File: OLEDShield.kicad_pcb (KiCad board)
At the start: 2 copper layers, 14 parts, among them P1 CONN_5X2, P2 CONN_5X2

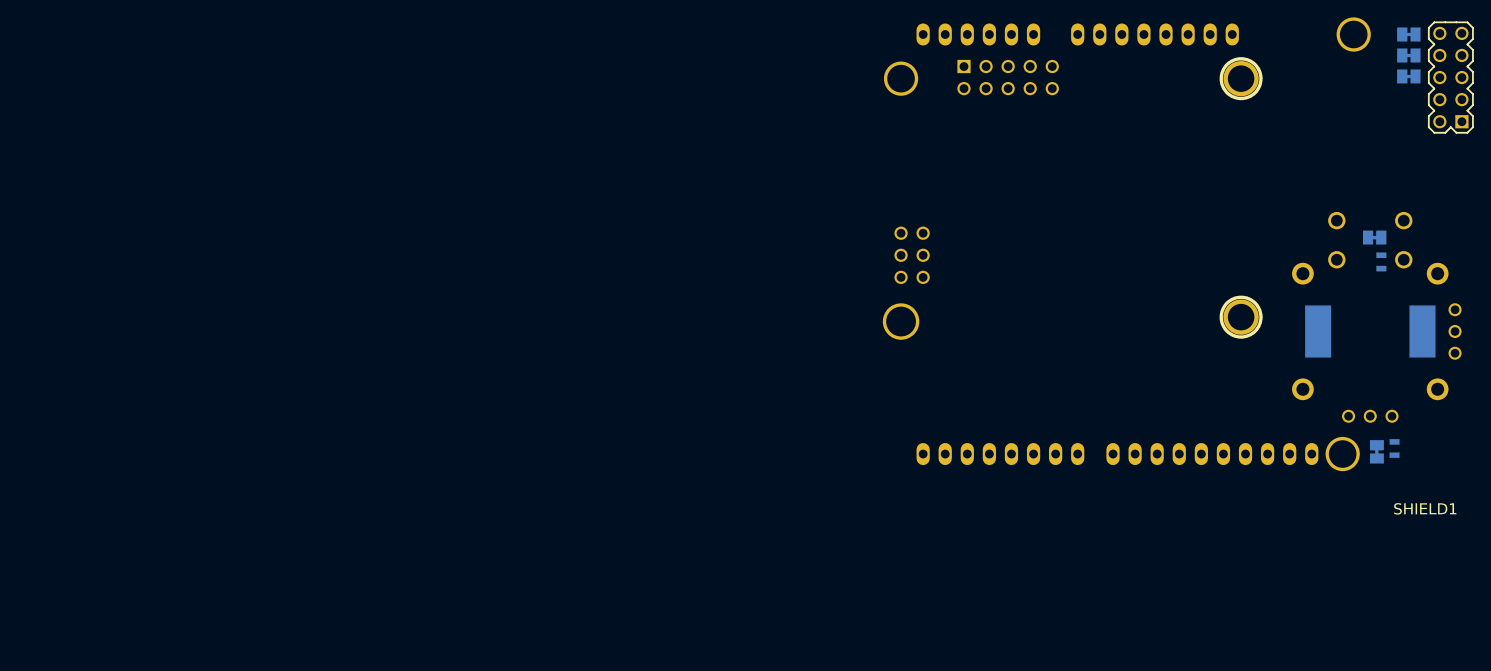
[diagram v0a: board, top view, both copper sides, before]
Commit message: Board largely done, no silkscreen labels yet
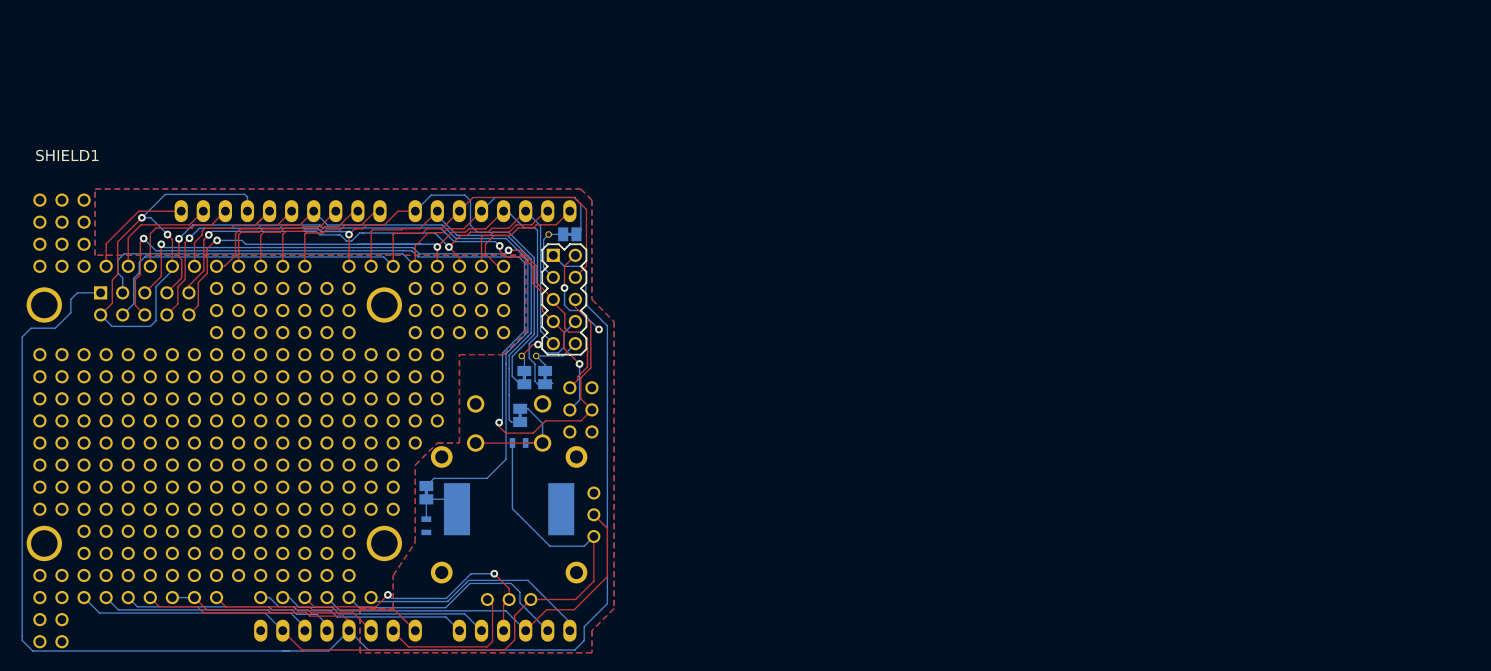
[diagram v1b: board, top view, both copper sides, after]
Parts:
- removed the 1PIN at (359.2, 238.3)
- added 1PIN: P***, 1pin_prototyping, F.Cu at (221.0, 227.3)
- added 1PIN: P***, 1pin_prototyping, F.Cu at (259.1, 252.7)
- added 1PIN: P***, 1pin_prototyping, F.Cu at (243.8, 255.3)
- added 1PIN: P***, 1pin_prototyping, F.Cu at (243.8, 247.7)
- added 1PIN: P***, 1pin_prototyping, F.Cu at (238.8, 247.7)
- added 1PIN: P***, 1pin_prototyping, F.Cu at (241.3, 247.7)
- added 1PIN: P***, 1pin_prototyping, F.Cu at (246.4, 247.7)
- added 1PIN: P***, 1pin_prototyping, F.Cu at (248.9, 247.7)
- added 1PIN: P***, 1pin_prototyping, F.Cu at (251.5, 247.7)
- added 1PIN: P***, 1pin_prototyping, F.Cu at (254.0, 247.7)
- added 1PIN: P***, 1pin_prototyping, F.Cu at (254.0, 250.2)
- added 1PIN: P***, 1pin_prototyping, F.Cu at (251.5, 250.2)
- added 1PIN: P***, 1pin_prototyping, F.Cu at (259.1, 250.2)
- added 1PIN: P***, 1pin_prototyping, F.Cu at (248.9, 250.2)
- added 1PIN: P***, 1pin_prototyping, F.Cu at (246.4, 250.2)
- added 1PIN: P***, 1pin_prototyping, F.Cu at (243.8, 250.2)
- added 1PIN: P***, 1pin_prototyping, F.Cu at (241.3, 250.2)
- added 1PIN: P***, 1pin_prototyping, F.Cu at (238.8, 250.2)
- added 1PIN: P***, 1pin_prototyping, F.Cu at (238.8, 252.7)
- added 1PIN: P***, 1pin_prototyping, F.Cu at (241.3, 252.7)
- added 1PIN: P***, 1pin_prototyping, F.Cu at (243.8, 252.7)
- added 1PIN: P***, 1pin_prototyping, F.Cu at (246.4, 252.7)
- added 1PIN: P***, 1pin_prototyping, F.Cu at (248.9, 252.7)
- added 1PIN: P***, 1pin_prototyping, F.Cu at (259.1, 247.7)
- added 1PIN: P***, 1pin_prototyping, F.Cu at (251.5, 252.7)
- added 1PIN: P***, 1pin_prototyping, F.Cu at (254.0, 252.7)
- added 1PIN: P***, 1pin_prototyping, F.Cu at (236.2, 247.7)
- added 1PIN: P***, 1pin_prototyping, F.Cu at (233.7, 247.7)
- added 1PIN: P***, 1pin_prototyping, F.Cu at (231.1, 247.7)
- added 1PIN: P***, 1pin_prototyping, F.Cu at (228.6, 247.7)
- added 1PIN: P***, 1pin_prototyping, F.Cu at (226.1, 247.7)
- added 1PIN: P***, 1pin_prototyping, F.Cu at (223.5, 247.7)
- added 1PIN: P***, 1pin_prototyping, F.Cu at (221.0, 247.7)
- added 1PIN: P***, 1pin_prototyping, F.Cu at (221.0, 245.1)
- added 1PIN: P***, 1pin_prototyping, F.Cu at (259.1, 255.3)
- added 1PIN: P***, 1pin_prototyping, F.Cu at (223.5, 245.1)
- added 1PIN: P***, 1pin_prototyping, F.Cu at (226.1, 245.1)
- added 1PIN: P***, 1pin_prototyping, F.Cu at (228.6, 245.1)
- added 1PIN: P***, 1pin_prototyping, F.Cu at (231.1, 245.1)
- added 1PIN: P***, 1pin_prototyping, F.Cu at (233.7, 245.1)
- added 1PIN: P***, 1pin_prototyping, F.Cu at (236.2, 245.1)
- added 1PIN: P***, 1pin_prototyping, F.Cu at (236.2, 242.6)
- added 1PIN: P***, 1pin_prototyping, F.Cu at (233.7, 242.6)
- added 1PIN: P***, 1pin_prototyping, F.Cu at (231.1, 242.6)
- added 1PIN: P***, 1pin_prototyping, F.Cu at (228.6, 242.6)
- added 1PIN: P***, 1pin_prototyping, F.Cu at (259.1, 257.8)
- added 1PIN: P***, 1pin_prototyping, F.Cu at (223.5, 242.6)
- added 1PIN: P***, 1pin_prototyping, F.Cu at (221.0, 242.6)
- added 1PIN: P***, 1pin_prototyping, F.Cu at (226.1, 242.6)
- added 1PIN: P***, 1pin_prototyping, F.Cu at (259.1, 270.5)
- added 1PIN: P***, 1pin_prototyping, F.Cu at (256.5, 270.5)
- added 1PIN: P***, 1pin_prototyping, F.Cu at (254.0, 270.5)
- added 1PIN: P***, 1pin_prototyping, F.Cu at (251.5, 270.5)
- added 1PIN: P***, 1pin_prototyping, F.Cu at (248.9, 270.5)
- added 1PIN: P***, 1pin_prototyping, F.Cu at (246.4, 270.5)
- added 1PIN: P***, 1pin_prototyping, F.Cu at (241.3, 270.5)
- added 1PIN: P***, 1pin_prototyping, F.Cu at (259.1, 260.4)
- added 1PIN: P***, 1pin_prototyping, F.Cu at (238.8, 270.5)
- added 1PIN: P***, 1pin_prototyping, F.Cu at (236.2, 270.5)
- added 1PIN: P***, 1pin_prototyping, F.Cu at (233.7, 270.5)
- added 1PIN: P***, 1pin_prototyping, F.Cu at (231.1, 270.5)
- added 1PIN: P***, 1pin_prototyping, F.Cu at (228.6, 270.5)
- added 1PIN: P***, 1pin_prototyping, F.Cu at (226.1, 270.5)
- added 1PIN: P***, 1pin_prototyping, F.Cu at (274.3, 232.4)
- added 1PIN: P***, 1pin_prototyping, F.Cu at (271.8, 232.4)
- added 1PIN: P***, 1pin_prototyping, F.Cu at (269.2, 232.4)
- added 1PIN: P***, 1pin_prototyping, F.Cu at (266.7, 232.4)
- added 1PIN: P***, 1pin_prototyping, F.Cu at (261.6, 260.4)
- added 1PIN: P***, 1pin_prototyping, F.Cu at (264.2, 232.4)
- added 1PIN: P***, 1pin_prototyping, F.Cu at (261.6, 232.4)
- added 1PIN: P***, 1pin_prototyping, F.Cu at (259.1, 232.4)
- added 1PIN: P***, 1pin_prototyping, F.Cu at (256.5, 232.4)
- added 1PIN: P***, 1pin_prototyping, F.Cu at (251.5, 232.4)
- added 1PIN: P***, 1pin_prototyping, F.Cu at (248.9, 232.4)
- added 1PIN: P***, 1pin_prototyping, F.Cu at (246.4, 232.4)
- added 1PIN: P***, 1pin_prototyping, F.Cu at (243.8, 232.4)
- added 1PIN: P***, 1pin_prototyping, F.Cu at (241.3, 232.4)
- added 1PIN: P***, 1pin_prototyping, F.Cu at (238.8, 232.4)
- added 1PIN: P***, 1pin_prototyping, F.Cu at (261.6, 257.8)
- added 1PIN: P***, 1pin_prototyping, F.Cu at (231.1, 232.4)
- added 1PIN: P***, 1pin_prototyping, F.Cu at (228.6, 232.4)
- added 1PIN: P***, 1pin_prototyping, F.Cu at (233.7, 232.4)
- added 1PIN: P***, 1pin_prototyping, F.Cu at (236.2, 232.4)
- added 1PIN: P***, 1pin, B.Cu at (221.5, 264.3)
- added 1PIN: P***, 1pin, B.Cu at (260.6, 264.3)
- added 1PIN: P***, 1pin, B.Cu at (260.6, 236.9)
- added 1PIN: P***, 1pin_prototyping, F.Cu at (241.3, 234.9)
- added 1PIN: P***, 1pin_prototyping, F.Cu at (243.8, 234.9)
- added 1PIN: P***, 1pin_prototyping, F.Cu at (261.6, 255.3)
- added 1PIN: P***, 1pin_prototyping, F.Cu at (246.4, 234.9)
- added 1PIN: P***, 1pin_prototyping, F.Cu at (248.9, 234.9)
- added 1PIN: P***, 1pin_prototyping, F.Cu at (251.5, 234.9)
- added 1PIN: P***, 1pin_prototyping, F.Cu at (254.0, 234.9)
- added 1PIN: P***, 1pin_prototyping, F.Cu at (256.5, 234.9)
- added 1PIN: P***, 1pin_prototyping, F.Cu at (241.3, 237.5)
- added 1PIN: P***, 1pin_prototyping, F.Cu at (243.8, 237.5)
- added 1PIN: P***, 1pin_prototyping, F.Cu at (246.4, 237.5)
- added 1PIN: P***, 1pin_prototyping, F.Cu at (248.9, 237.5)
- added 1PIN: P***, 1pin_prototyping, F.Cu at (251.5, 237.5)
- added 1PIN: P***, 1pin_prototyping, F.Cu at (261.6, 247.7)
- added 1PIN: P***, 1pin_prototyping, F.Cu at (254.0, 237.5)
- added 1PIN: P***, 1pin_prototyping, F.Cu at (256.5, 237.5)
- added 1PIN: P***, 1pin_prototyping, F.Cu at (241.3, 240.0)
- added 1PIN: P***, 1pin_prototyping, F.Cu at (243.8, 240.0)
- added 1PIN: P***, 1pin_prototyping, F.Cu at (246.4, 240.0)
- added 1PIN: P***, 1pin_prototyping, F.Cu at (248.9, 240.0)
- added 1PIN: P***, 1pin_prototyping, F.Cu at (251.5, 240.0)
- added 1PIN: P***, 1pin_prototyping, F.Cu at (254.0, 240.0)
- added 1PIN: P***, 1pin_prototyping, F.Cu at (256.5, 240.0)
- added 1PIN: P***, 1pin_prototyping, F.Cu at (226.1, 250.2)
- added 1PIN: P***, 1pin_prototyping, F.Cu at (223.5, 227.3)
- added 1PIN: P***, 1pin_prototyping, F.Cu at (261.6, 250.2)
- added 1PIN: P***, 1pin_prototyping, F.Cu at (221.0, 250.2)
- added 1PIN: P***, 1pin_prototyping, F.Cu at (223.5, 250.2)
- added 1PIN: P***, 1pin_prototyping, F.Cu at (228.6, 250.2)
- added 1PIN: P***, 1pin_prototyping, F.Cu at (231.1, 250.2)
- added 1PIN: P***, 1pin_prototyping, F.Cu at (233.7, 250.2)
- added 1PIN: P***, 1pin_prototyping, F.Cu at (236.2, 250.2)
- added 1PIN: P***, 1pin_prototyping, F.Cu at (238.8, 242.6)
- added 1PIN: P***, 1pin_prototyping, F.Cu at (241.3, 242.6)
- added 1PIN: P***, 1pin_prototyping, F.Cu at (243.8, 242.6)
- added 1PIN: P***, 1pin_prototyping, F.Cu at (246.4, 242.6)
- added 1PIN: P***, 1pin_prototyping, F.Cu at (261.6, 252.7)
- added 1PIN: P***, 1pin_prototyping, F.Cu at (248.9, 242.6)
- added 1PIN: P***, 1pin_prototyping, F.Cu at (251.5, 242.6)
- added 1PIN: P***, 1pin_prototyping, F.Cu at (254.0, 242.6)
- added 1PIN: P***, 1pin_prototyping, F.Cu at (256.5, 242.6)
- added 1PIN: P***, 1pin_prototyping, F.Cu at (264.2, 240.0)
- added 1PIN: P***, 1pin_prototyping, F.Cu at (264.2, 237.5)
- added 1PIN: P***, 1pin_prototyping, F.Cu at (264.2, 234.9)
- added 1PIN: P***, 1pin_prototyping, F.Cu at (266.7, 234.9)
- added 1PIN: P***, 1pin_prototyping, F.Cu at (266.7, 237.5)
- added 1PIN: P***, 1pin_prototyping, F.Cu at (266.7, 240.0)
- added 1PIN: P***, 1pin_prototyping, F.Cu at (256.5, 252.7)
- added 1PIN: P***, 1pin_prototyping, F.Cu at (269.2, 240.0)
- added 1PIN: P***, 1pin_prototyping, F.Cu at (269.2, 237.5)
- added 1PIN: P***, 1pin_prototyping, F.Cu at (269.2, 234.9)
- added 1PIN: P***, 1pin_prototyping, F.Cu at (271.8, 234.9)
- added 1PIN: P***, 1pin_prototyping, F.Cu at (271.8, 237.5)
- added 1PIN: P***, 1pin_prototyping, F.Cu at (271.8, 240.0)
- added 1PIN: P***, 1pin_prototyping, F.Cu at (274.3, 240.0)
- added 1PIN: P***, 1pin_prototyping, F.Cu at (274.3, 237.5)
- added 1PIN: P***, 1pin_prototyping, F.Cu at (274.3, 234.9)
- added 1PIN: P***, 1pin_prototyping, F.Cu at (266.7, 242.6)
- added 1PIN: P***, 1pin_prototyping, F.Cu at (256.5, 250.2)
- added 1PIN: P***, 1pin_prototyping, F.Cu at (266.7, 245.1)
- added 1PIN: P***, 1pin_prototyping, F.Cu at (266.7, 247.7)
- added 1PIN: P***, 1pin_prototyping, F.Cu at (266.7, 250.2)
- added 1PIN: P***, 1pin_prototyping, F.Cu at (264.2, 242.6)
- added 1PIN: P***, 1pin_prototyping, F.Cu at (264.2, 245.1)
- added 1PIN: P***, 1pin_prototyping, F.Cu at (264.2, 247.7)
- added 1PIN: P***, 1pin_prototyping, F.Cu at (264.2, 250.2)
- added 1PIN: P***, 1pin_prototyping, F.Cu at (264.2, 252.7)
- added 1PIN: P***, 1pin_prototyping, F.Cu at (261.6, 242.6)
- added 1PIN: P***, 1pin_prototyping, F.Cu at (259.1, 242.6)
- added 1PIN: P***, 1pin_prototyping, F.Cu at (256.5, 247.7)
- added 1PIN: P***, 1pin_prototyping, F.Cu at (261.6, 245.1)
- added 1PIN: P***, 1pin_prototyping, F.Cu at (259.1, 245.1)
- added 1PIN: P***, 1pin_prototyping, F.Cu at (256.5, 245.1)
- added 1PIN: P***, 1pin_prototyping, F.Cu at (254.0, 245.1)
- added 1PIN: P***, 1pin_prototyping, F.Cu at (251.5, 245.1)
- added 1PIN: P***, 1pin_prototyping, F.Cu at (248.9, 245.1)
- added 1PIN: P***, 1pin_prototyping, F.Cu at (246.4, 245.1)
- added 1PIN: P***, 1pin_prototyping, F.Cu at (243.8, 245.1)
- added 1PIN: P***, 1pin_prototyping, F.Cu at (241.3, 245.1)
- added 1PIN: P***, 1pin_prototyping, F.Cu at (238.8, 245.1)
- added 1PIN: P***, 1pin_prototyping, F.Cu at (256.5, 255.3)
- added 1PIN: P***, 1pin_prototyping, F.Cu at (236.2, 252.7)
- added 1PIN: P***, 1pin_prototyping, F.Cu at (233.7, 252.7)
- added 1PIN: P***, 1pin_prototyping, F.Cu at (231.1, 252.7)
- added 1PIN: P***, 1pin_prototyping, F.Cu at (228.6, 252.7)
- added 1PIN: P***, 1pin_prototyping, F.Cu at (226.1, 252.7)
- added 1PIN: P***, 1pin_prototyping, F.Cu at (223.5, 252.7)
- added 1PIN: P***, 1pin_prototyping, F.Cu at (221.0, 252.7)
- added 1PIN: P***, 1pin_prototyping, F.Cu at (221.0, 255.3)
- added 1PIN: P***, 1pin_prototyping, F.Cu at (223.5, 255.3)
- added 1PIN: P***, 1pin_prototyping, F.Cu at (226.1, 255.3)
- added 1PIN: P***, 1pin_prototyping, F.Cu at (256.5, 257.8)
- added 1PIN: P***, 1pin_prototyping, F.Cu at (228.6, 255.3)
- added 1PIN: P***, 1pin_prototyping, F.Cu at (231.1, 255.3)
- added 1PIN: P***, 1pin_prototyping, F.Cu at (233.7, 255.3)
- added 1PIN: P***, 1pin_prototyping, F.Cu at (236.2, 255.3)
- added 1PIN: P***, 1pin_prototyping, F.Cu at (226.1, 268.0)
- added 1PIN: P***, 1pin_prototyping, F.Cu at (226.1, 232.4)
- added 1PIN: P***, 1pin_prototyping, F.Cu at (223.5, 232.4)
- added 1PIN: P***, 1pin_prototyping, F.Cu at (221.0, 232.4)
- added 1PIN: P***, 1pin_prototyping, F.Cu at (223.5, 268.0)
- added 1PIN: P***, 1pin_prototyping, F.Cu at (221.0, 268.0)
- added 1PIN: P***, 1pin_prototyping, F.Cu at (256.5, 260.4)
- added 1PIN: P***, 1pin_prototyping, F.Cu at (221.0, 270.5)
- added 1PIN: P***, 1pin_prototyping, F.Cu at (223.5, 270.5)
- added 1PIN: P***, 1pin_prototyping, F.Cu at (223.5, 273.1)
- added 1PIN: P***, 1pin_prototyping, F.Cu at (221.0, 273.1)
- added 1PIN: P***, 1pin_prototyping, F.Cu at (223.5, 275.6)
- added 1PIN: P***, 1pin_prototyping, F.Cu at (221.0, 275.6)
- added 1PIN: P***, 1pin_prototyping, F.Cu at (256.5, 265.4)
- added 1PIN: P***, 1pin_prototyping, F.Cu at (256.5, 262.9)
- added 1PIN: P***, 1pin_prototyping, F.Cu at (226.1, 227.3)
- added 1PIN: P***, 1pin_prototyping, F.Cu at (256.5, 268.0)
- added 1PIN: P***, 1pin_prototyping, F.Cu at (236.2, 268.0)
- added 1PIN: P***, 1pin_prototyping, F.Cu at (233.7, 268.0)
- added 1PIN: P***, 1pin_prototyping, F.Cu at (231.1, 268.0)
- added 1PIN: P***, 1pin_prototyping, F.Cu at (228.6, 268.0)
- added 1PIN: P***, 1pin_prototyping, F.Cu at (254.0, 268.0)
- added 1PIN: P***, 1pin_prototyping, F.Cu at (251.5, 268.0)
- added 1PIN: P***, 1pin_prototyping, F.Cu at (248.9, 268.0)
- added 1PIN: P***, 1pin_prototyping, F.Cu at (246.4, 268.0)
- added 1PIN: P***, 1pin_prototyping, F.Cu at (243.8, 268.0)
- added 1PIN: P***, 1pin_prototyping, F.Cu at (226.1, 224.8)
- added 1PIN: P***, 1pin_prototyping, F.Cu at (241.3, 268.0)
- added 1PIN: P***, 1pin_prototyping, F.Cu at (238.8, 268.0)
- added 1PIN: P***, 1pin_prototyping, F.Cu at (254.0, 262.9)
- added 1PIN: P***, 1pin_prototyping, F.Cu at (251.5, 262.9)
- added 1PIN: P***, 1pin_prototyping, F.Cu at (248.9, 262.9)
- added 1PIN: P***, 1pin_prototyping, F.Cu at (246.4, 262.9)
- added 1PIN: P***, 1pin_prototyping, F.Cu at (243.8, 262.9)
- added 1PIN: P***, 1pin_prototyping, F.Cu at (241.3, 262.9)
- added 1PIN: P***, 1pin_prototyping, F.Cu at (238.8, 262.9)
- added 1PIN: P***, 1pin_prototyping, F.Cu at (238.8, 265.4)
- added 1PIN: P***, 1pin_prototyping, F.Cu at (223.5, 224.8)
- added 1PIN: P***, 1pin_prototyping, F.Cu at (241.3, 265.4)
- added 1PIN: P***, 1pin_prototyping, F.Cu at (243.8, 265.4)
- added 1PIN: P***, 1pin_prototyping, F.Cu at (246.4, 265.4)
- added 1PIN: P***, 1pin_prototyping, F.Cu at (248.9, 265.4)
- added 1PIN: P***, 1pin_prototyping, F.Cu at (251.5, 265.4)
- added 1PIN: P***, 1pin_prototyping, F.Cu at (254.0, 265.4)
- added 1PIN: P***, 1pin_prototyping, F.Cu at (236.2, 262.9)
- added 1PIN: P***, 1pin_prototyping, F.Cu at (233.7, 262.9)
- added 1PIN: P***, 1pin_prototyping, F.Cu at (231.1, 262.9)
- added 1PIN: P***, 1pin_prototyping, F.Cu at (228.6, 262.9)
- added 1PIN: P***, 1pin_prototyping, F.Cu at (221.0, 224.8)
- added 1PIN: P***, 1pin_prototyping, F.Cu at (226.1, 262.9)
- added 1PIN: P***, 1pin_prototyping, F.Cu at (226.1, 265.4)
- added 1PIN: P***, 1pin_prototyping, F.Cu at (228.6, 265.4)
- added 1PIN: P***, 1pin_prototyping, F.Cu at (231.1, 265.4)
- added 1PIN: P***, 1pin_prototyping, F.Cu at (233.7, 265.4)
- added 1PIN: P***, 1pin_prototyping, F.Cu at (236.2, 265.4)
- added 1PIN: P***, 1pin_prototyping, F.Cu at (236.2, 260.4)
- added 1PIN: P***, 1pin_prototyping, F.Cu at (233.7, 260.4)
- added 1PIN: P***, 1pin_prototyping, F.Cu at (231.1, 260.4)
- added 1PIN: P***, 1pin_prototyping, F.Cu at (228.6, 260.4)
- added 1PIN: P***, 1pin_prototyping, F.Cu at (221.0, 229.9)
- added 1PIN: P***, 1pin_prototyping, F.Cu at (226.1, 260.4)
- added 1PIN: P***, 1pin_prototyping, F.Cu at (223.5, 260.4)
- added 1PIN: P***, 1pin_prototyping, F.Cu at (221.0, 260.4)
- added 1PIN: P***, 1pin_prototyping, F.Cu at (221.0, 257.8)
- added 1PIN: P***, 1pin_prototyping, F.Cu at (223.5, 257.8)
- added 1PIN: P***, 1pin_prototyping, F.Cu at (226.1, 257.8)
- added 1PIN: P***, 1pin_prototyping, F.Cu at (228.6, 257.8)
- added 1PIN: P***, 1pin_prototyping, F.Cu at (231.1, 257.8)
- added 1PIN: P***, 1pin_prototyping, F.Cu at (233.7, 257.8)
- added 1PIN: P***, 1pin_prototyping, F.Cu at (236.2, 257.8)
- added 1PIN: P***, 1pin_prototyping, F.Cu at (223.5, 229.9)
- added 1PIN: P***, 1pin_prototyping, F.Cu at (254.0, 260.4)
- added 1PIN: P***, 1pin_prototyping, F.Cu at (251.5, 260.4)
- added 1PIN: P***, 1pin_prototyping, F.Cu at (248.9, 260.4)
- added 1PIN: P***, 1pin_prototyping, F.Cu at (246.4, 260.4)
- added 1PIN: P***, 1pin_prototyping, F.Cu at (243.8, 260.4)
- added 1PIN: P***, 1pin_prototyping, F.Cu at (241.3, 260.4)
- added 1PIN: P***, 1pin_prototyping, F.Cu at (238.8, 260.4)
- added 1PIN: P***, 1pin_prototyping, F.Cu at (238.8, 257.8)
- added 1PIN: P***, 1pin_prototyping, F.Cu at (241.3, 257.8)
- added 1PIN: P***, 1pin_prototyping, F.Cu at (243.8, 257.8)
- added 1PIN: P***, 1pin_prototyping, F.Cu at (226.1, 229.9)
- added 1PIN: P***, 1pin_prototyping, F.Cu at (246.4, 257.8)
- added 1PIN: P***, 1pin_prototyping, F.Cu at (248.9, 257.8)
- added 1PIN: P***, 1pin_prototyping, F.Cu at (251.5, 257.8)
- added 1PIN: P***, 1pin_prototyping, F.Cu at (254.0, 257.8)
- added 1PIN: P***, 1pin_prototyping, F.Cu at (254.0, 255.3)
- added 1PIN: P***, 1pin_prototyping, F.Cu at (251.5, 255.3)
- added 1PIN: P***, 1pin_prototyping, F.Cu at (248.9, 255.3)
- added 1PIN: P***, 1pin_prototyping, F.Cu at (246.4, 255.3)
- added 1PIN: P***, 1pin_prototyping, F.Cu at (241.3, 255.3)
- added 1PIN: P***, 1pin_prototyping, F.Cu at (238.8, 255.3)
- added P3: CONN_1, 1pin_prototyping_mini, F.Cu at (278.1, 242.7)
- added P4: CONN_1, 1pin_prototyping_mini, F.Cu at (276.4, 242.7)
- added P5: CONN_1, 1pin_prototyping_mini, F.Cu at (279.5, 228.8)
- 1PIN: moved to B.Cu
- moved SHIELD1 183.1 mm to (218.4, 276.9), turned to 0 degrees
- moved 1PIN 140.1 mm to (221.5, 236.9), turned to 180 degrees
- moved R1 111.7 mm to (265.4, 262.3)
- moved SJ1 109.4 mm to (265.4, 258.4), turned to 270 degrees
- moved SJ4 108.3 mm to (276.7, 245.2), turned to 270 degrees
- moved SJ5 106.9 mm to (279.1, 245.2), turned to 270 degrees
- moved P2 105.6 mm to (280.0, 231.1), turned to 270 degrees
- moved P1 102.7 mm to (228.0, 235.5)
- moved R2 101.4 mm to (276.1, 252.7), turned to 0 degrees
- moved JOYSTICK1 101.3 mm to (275.0, 261.0)
- moved PIEZO1 101.1 mm to (275.0, 260.4)
- moved SJ2 100.4 mm to (276.2, 249.6), turned to 90 degrees
- moved SJ3 98.2 mm to (281.9, 228.7), turned to 180 degrees
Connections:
- net /JOY_BUTTON renamed /D6
- net /JOY_X renamed /AD2_JOY_X
- net /JOY_Y renamed /AD3_JOY_Y
- net /PIEZO renamed /D11
- net N-0000024 renamed /RHS_OLED_nCS
- net N-0000035 renamed /RHS_OLED_nRST
- P2 pad 3: N-0000011 (its old number) -> /RHS_uSD_nCS
- SHIELD1 pad 0: N-0000022 (its old number) -> /D0
- SHIELD1 pad 1: N-0000021 -> /D1
- SHIELD1 pad 10: N-0000023 -> /D10
- SHIELD1 pad 12: N-0000029 -> /D12
- SHIELD1 pad 13: N-0000028 -> /D13
- SHIELD1 pad 3V3: N-0000017 -> /3V3
- SHIELD1 pad 8: N-0000025 (its old number) -> /D8
- SHIELD1 pad 9: N-0000012 -> /D9
- SHIELD1 pad AD0: N-0000018 -> /AD0
- SHIELD1 pad AD1: N-0000032 -> /AD1
- SHIELD1 pad AD4: N-0000019 -> /AD4
- SHIELD1 pad AD5: N-0000020 -> /AD5
- SHIELD1 pad AREF: N-0000013 -> /AREF
- SHIELD1 pad RST: N-0000016 -> /RST
- SHIELD1 pad SCL: N-0000026 (its old number) -> /SCL
- SHIELD1 pad SDA: N-0000027 -> /SDA
- SHIELD1 pad V_IN: N-0000014 -> /V_IN
- SJ3 pad 2: N-0000011 (its old number) -> /RHS_uSD_nCS
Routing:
- net +5V: track 0.00 -> 189.4 mm
- net GND: track 0.00 -> 103.4 mm, vias 0 -> 4
- net /MOSI: track 0.00 -> 101.2 mm, vias 0 -> 2
- net VCC: track 0.00 -> 90.4 mm
- net /OLED_nRST: track 0.00 -> 81.0 mm, vias 0 -> 2
- net /OLED_nCS: track 0.00 -> 77.7 mm, vias 0 -> 2
- net /D11: track 0.00 -> 75.6 mm
- net /uSD_CD: track 0.00 -> 73.3 mm
- net /SCK: track 0.00 -> 70.0 mm, vias 0 -> 3
- net /MISO: track 0.00 -> 69.0 mm, vias 0 -> 2
- net /uSD_nCS: track 0.00 -> 66.9 mm
- net /OLED_DnC: track 0.00 -> 66.7 mm, vias 0 -> 2
- net /D6: track 0.00 -> 46.9 mm
- net /AD3_JOY_Y: track 0.00 -> 44.2 mm
- net /AD2_JOY_X: track 0.00 -> 31.7 mm, vias 0 -> 2
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- added copper zone on B.Cu, net GND
- added copper zone on F.Cu, net GND

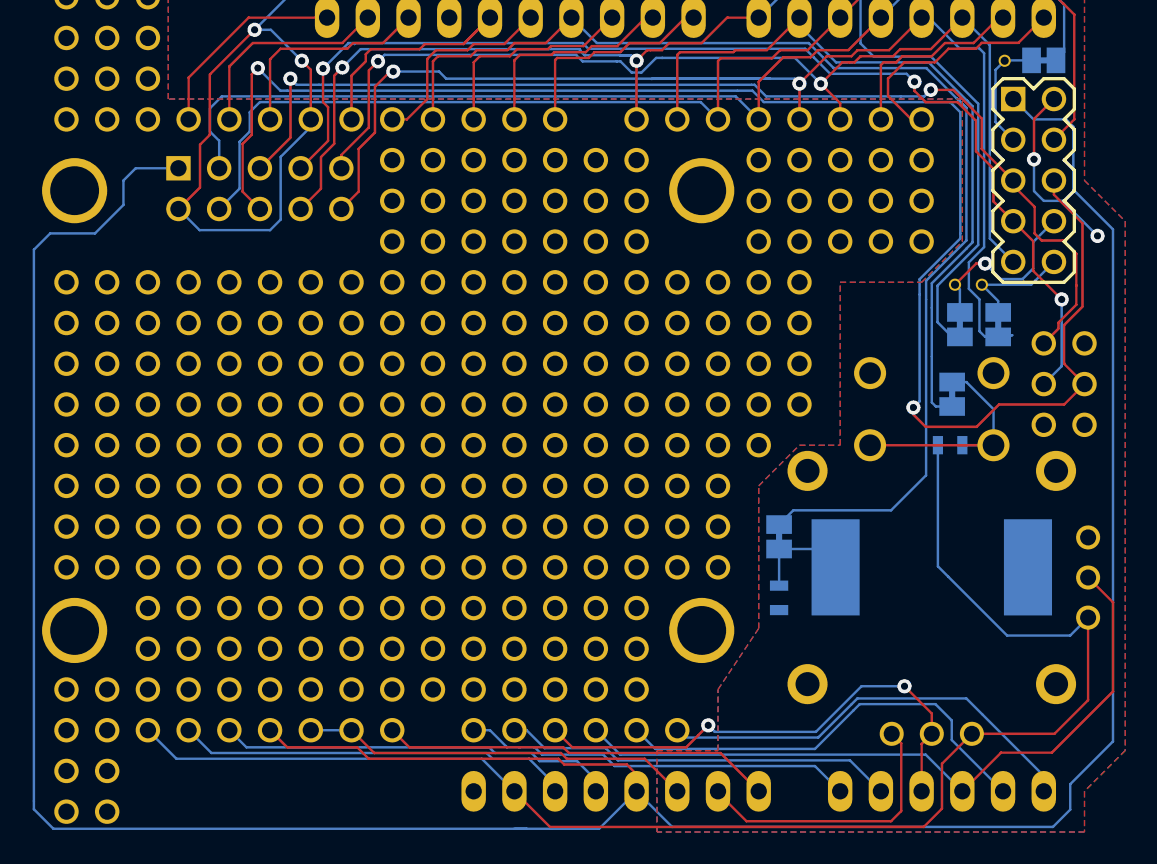
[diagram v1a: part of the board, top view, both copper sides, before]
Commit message: Fatten up power traces
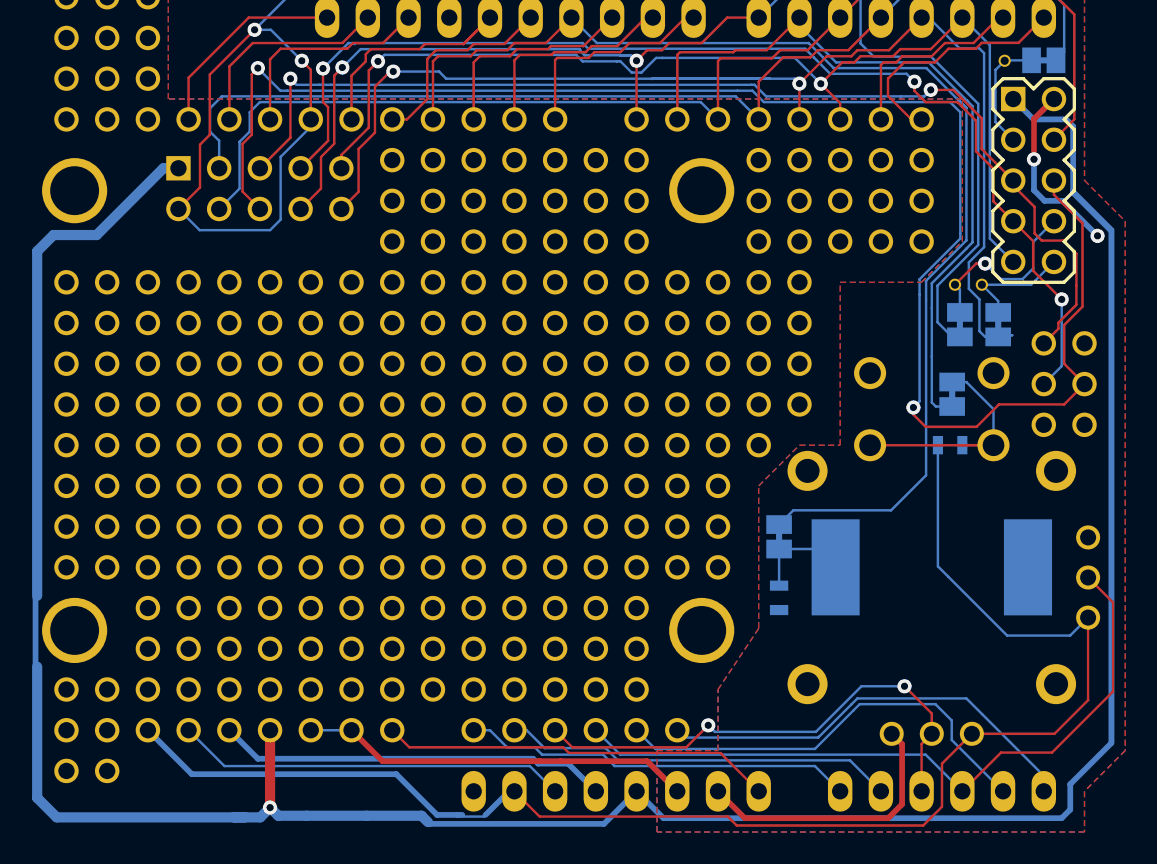
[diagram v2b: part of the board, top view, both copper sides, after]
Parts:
- removed the 1PIN at (223.5, 275.6)
- removed the 1PIN at (221.0, 275.6)
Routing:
- net +5V: track 189.4 -> 216.1 mm, vias 0 -> 1
- net GND: track 103.4 -> 108.6 mm
- net VCC: track 90.4 -> 91.9 mm
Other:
- net class Power added: clearance 0.2032, trace_width 0.3556, via_dia 0.889, via_drill 0.635

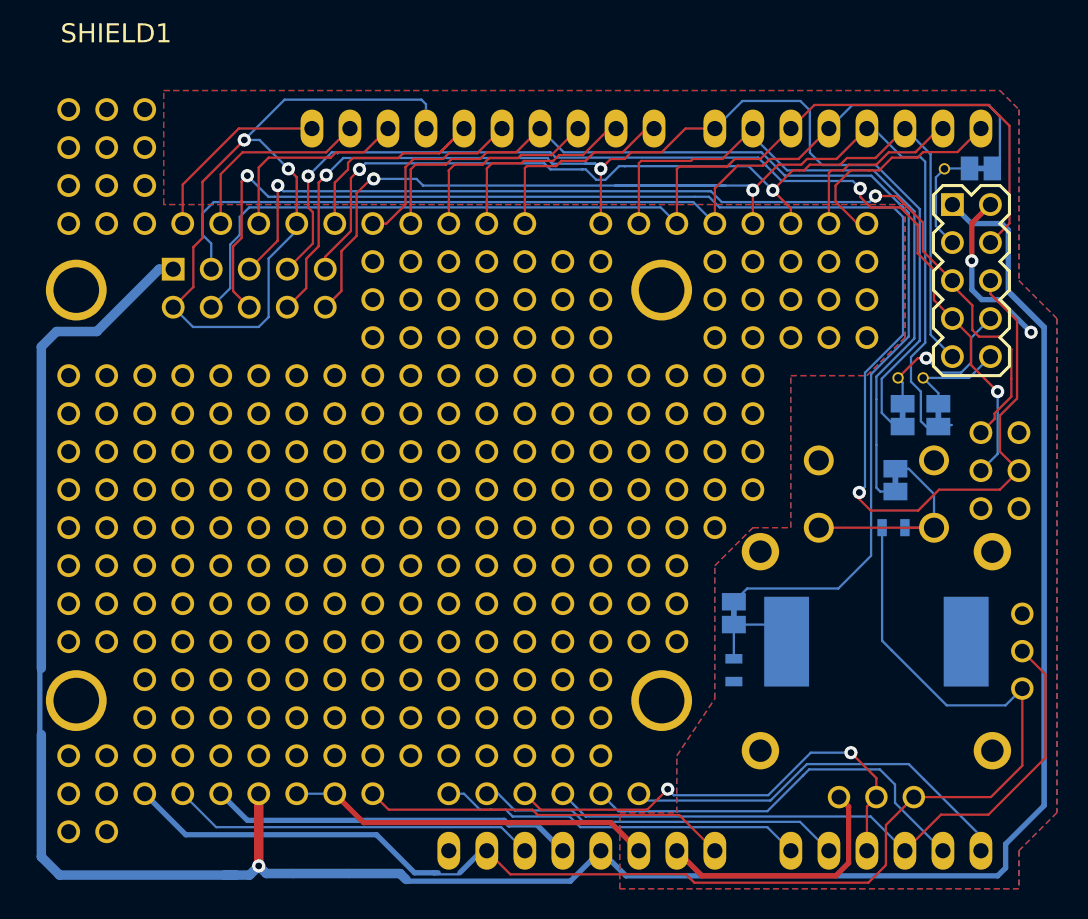
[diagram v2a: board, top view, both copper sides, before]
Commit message: Add power breakout areas, nearly all silkscreening
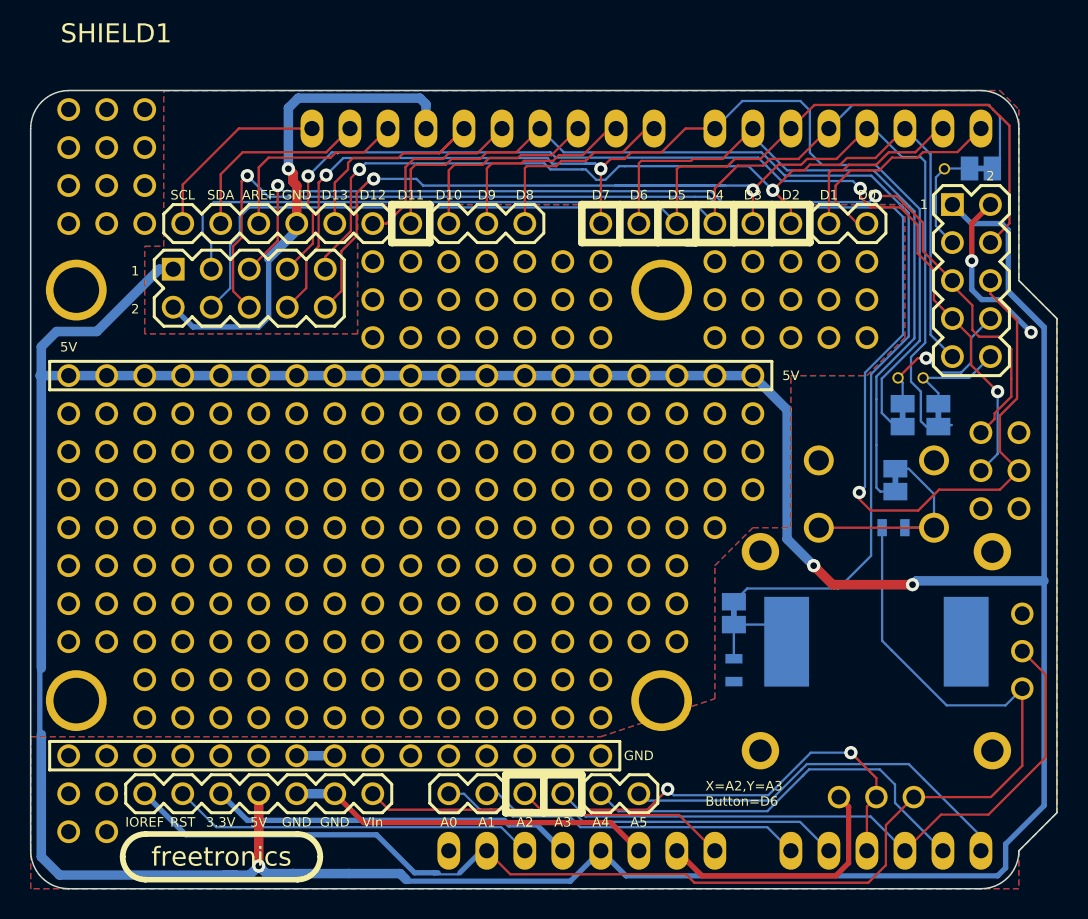
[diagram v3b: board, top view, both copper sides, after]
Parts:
- added ?: , LOGO_FREETRONICS, F.Cu at (231.2, 274.7)
- added ?: , LOGO_FREETRONICS, B.Cu at (231.2, 274.7)
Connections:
- 1PIN pad 1: (no net) -> GND (x15)
- 1PIN pad 1: (no net) -> +5V (x19)
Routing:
- net +5V: track 216.1 -> 295.7 mm, vias 1 -> 3
- net GND: track 108.6 -> 106.5 mm, vias 4 -> 3
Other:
- board outline added: 68.6 x 53.3 mm
- board text added: "1"
- board text added: "2"
- board text added: "3.3V"
- board text added: "5V"
- board text added: "A0"
- board text added: "A1"
- board text added: "A2"
- board text added: "A3"
- board text added: "A4"
- board text added: "A5"
- board text added: "AREF"
- board text added: "Button"
- board text added: "D0"
- board text added: "D1"
- board text added: "D10"
- board text added: "D11"
- board text added: "D12"
- board text added: "D13"
- board text added: "D2"
- board text added: "D3"
- board text added: "D4"
- board text added: "D5"
- board text added: "D6"
- board text added: "D7"
- board text added: "D8"
- board text added: "D9"
- board text added: "GND"
- board text added: "IOREF"
- board text added: "OLED nCS"
- board text added: "OLED nRST"
- board text added: "Piezo"
- board text added: "RST"
- board text added: "SCL"
- board text added: "SDA"
- board text added: "SJ1"
- board text added: "SJ2"
- board text added: "SJ3"
- board text added: "SJ4"
- board text added: "SJ5"
- board text added: "VIn"
- board text added: "X=A2,Y=A3 Button=D6"
- board text added: "uSD nCS"
